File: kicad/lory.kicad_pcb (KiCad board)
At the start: 2 copper layers, 123.5 x 85.3 mm, 22 parts, among them J1 MJ-4PP-9, SW10 SW_PUSH, SW11 SW_PUSH, SW12 SW_PUSH, SW14 SW_PUSH, SW15 SW_PUSH, SW16 SW_PUSH, SW17 SW_PUSH, SW18 SW_PUSH, SW2 SW_PUSH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

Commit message: Add wiring
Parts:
- J1: value MJ-4PP-9 -> TRRS; footprint kbd:MJ-4PP-9 -> broom:TRRS-PJ-DPB2
- moved J1 2.03 mm to (194.0, 94.5)
- moved RSW1 1.02 mm to (179.0, 94.5)
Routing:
- net row2: track 0.00 -> 124.2 mm, vias 0 -> 1
- net SCL: track 0.00 -> 113.7 mm, vias 0 -> 1
- net col4: track 0.00 -> 111.8 mm
- net col5: track 0.00 -> 97.9 mm
- net col1: track 0.00 -> 93.8 mm
- net row1: track 0.00 -> 92.6 mm, vias 0 -> 1
- net Net-(U1-Pad12): track 0.00 -> 85.0 mm, vias 0 -> 1
- net GND: track 0.00 -> 82.7 mm
- net SDA: track 0.00 -> 78.6 mm, vias 0 -> 1
- net col3: track 0.00 -> 76.7 mm
- net row3: track 0.00 -> 74.3 mm, vias 0 -> 1
- net data: track 0.00 -> 63.5 mm
- net reset: track 0.00 -> 61.5 mm, vias 0 -> 1
- net row0: track 0.00 -> 58.0 mm, vias 0 -> 1
- net Net-(U1-Pad14): track 0.00 -> 56.6 mm
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
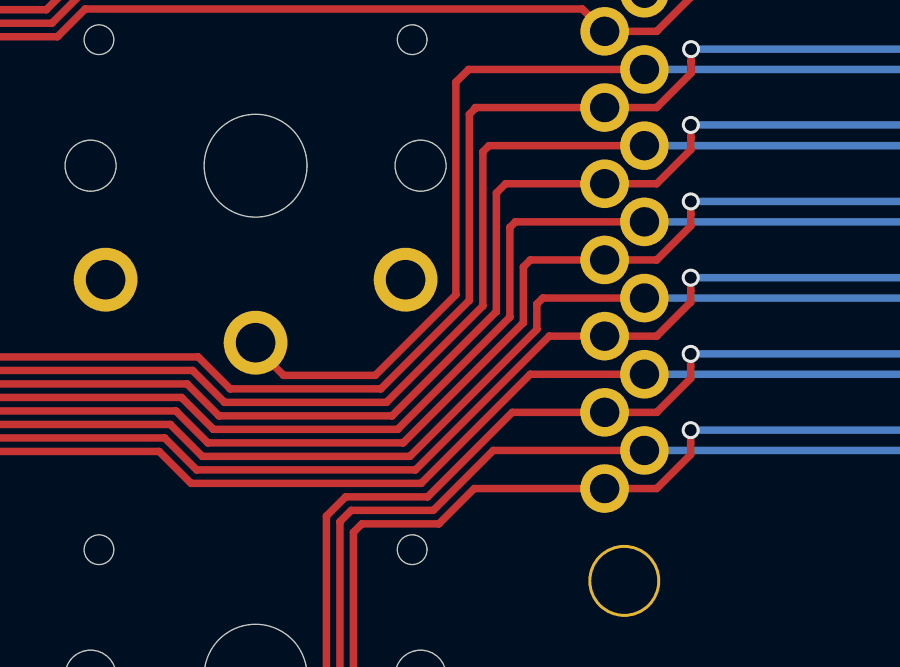
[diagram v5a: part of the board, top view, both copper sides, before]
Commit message: Delete leftover wiring
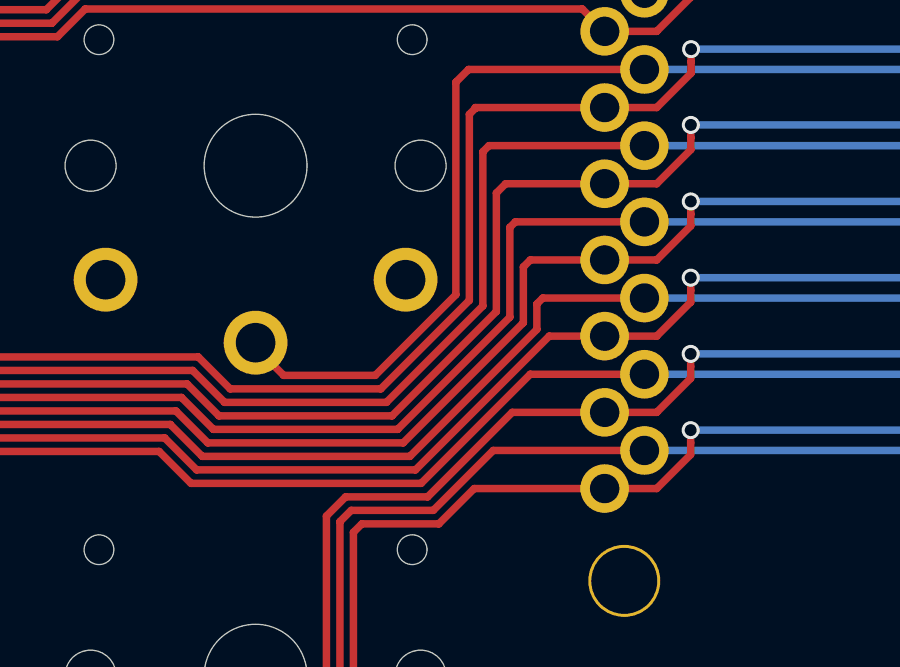
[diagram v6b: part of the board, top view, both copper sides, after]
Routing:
- net row2: track 124.2 -> 122.7 mm
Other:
- net class Default removed
